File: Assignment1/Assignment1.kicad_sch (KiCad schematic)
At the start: 22 parts, among them J1 Conn_01x02_Pin, J2 Conn_01x02_Pin, U1 TPS51386RJNR, U2 LD39200PU33R

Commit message: Update Assignment 1
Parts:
- removed Cbyp1: 470 nF, Capacitor_SMD:C_0603_1608Metric, symbol Device:C
- removed Cin1, Cout1: 10 uF, Capacitor_SMD:C_0603_1608Metric, symbol Device:C
- removed R_LDO_1: 56k, Resistor_SMD:R_0603_1608Metric, symbol Device:R
- removed R_LDO_2: 10k, Resistor_SMD:R_0603_1608Metric, symbol Device:R
- removed U2: LD39200PU33R, LD39200PU33R:SON95P300X300X100-7N, symbol LD39200PU33R:LD39200PU33R
- added C2, C3, C8: 22pF, Capacitor_SMD:C_1210_3225Metric, symbol Device:C
- added Cbyp2: 47 uF, Capacitor_SMD:C_1206_3216Metric, symbol Device:C
- added Cin2: 1 uF, Capacitor_SMD:C_0603_1608Metric, symbol Device:C
- added U3: ~, Package_TO_SOT_SMD:TO-263-3_TabPin2, symbol ProLib_pcs_2025-01-30:LM39300R-3.3
- C12: footprint Capacitor_SMD:C_0603_1608Metric -> Capacitor_SMD:C_1210_3225Metric
- C4, C5: footprint Capacitor_SMD:C_0603_1608Metric -> Capacitor_SMD:C_1206_3216Metric
- C7: value 100uF -> 22pF; footprint Capacitor_SMD:C_0603_1608Metric -> Capacitor_SMD:C_1210_3225Metric
- J1, J2: footprint Connector_PinSocket_2.54mm:PinSocket_1x02_P2.54mm_Vertical -> 5EHDVC-02P-KiCad:5EHDVC02P
- R4: value 150k -> 110k
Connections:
- net BuckStep_Vout: now also C2.1, C3.1, C8.1, Cin2.1, U3.1 (VIN)
- net Earth: now also C2.2, C3.2, C8.2, Cbyp2.2, Cin2.2, U3.2 (GND), U3.4 (TAB)
- net Vout: now also Cbyp2.1, U3.3 (VOUT)
- no-connect marks 2 -> 1
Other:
- note added: "LDO Module Converts 3.9V to 3.3V at maximum 2A"
- note removed: "LDO Module Converts 5.1V to 3.3V at maximum 2A"

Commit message: fix typo and update pcb
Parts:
- C2, C3, C7, C8: value 22pF -> 22uF
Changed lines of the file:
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@@
 		(on_board yes)
 		(dnp no)
-		(fields_autoplaced yes)
 		(property "Reference" "C8"
-			(at 123.19 90.1699 0)
+			(at 120.904 89.154 0)
 			(effects
 				(font
@@
 			)
 		)
-		(property "Value" "22pF"
-			(at 123.19 92.7099 0)
+		(property "Value" "22uF"
+			(at 120.396 93.726 0)
 			(effects
 				(font
@@
 		(on_board yes)
 		(dnp no)
-		(fields_autoplaced yes)
 		(property "Reference" "C7"
-			(at 116.84 90.1699 0)
+			(at 113.792 89.408 0)
 			(effects
 				(font
@@
 			)
 		)
-		(property "Value" "22pF"
-			(at 116.84 92.7099 0)
+		(property "Value" "22uF"
+			(at 113.538 93.726 0)
 			(effects
 				(font
@@
 		(on_board yes)
 		(dnp no)
-		(fields_autoplaced yes)
 		(property "Reference" "C3"
-			(at 138.43 90.1699 0)
+			(at 136.398 89.154 0)
 			(effects
 				(font
@@
 			)
 		)
-		(property "Value" "22pF"
-			(at 138.43 92.7099 0)
+		(property "Value" "22uF"
+			(at 136.398 93.98 0)
 			(effects
 				(font
@@
 		(on_board yes)
 		(dnp no)
-		(fields_autoplaced yes)
 		(property "Reference" "C2"
-			(at 129.54 90.1699 0)
+			(at 127.254 89.154 0)
 			(effects
 				(font
@@
 			)
 		)
-		(property "Value" "22pF"
-			(at 129.54 92.7099 0)
+		(property "Value" "22uF"
+			(at 126.746 93.726 0)
 			(effects
 				(font

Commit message: reformat
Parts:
- C13, Cin2: value 1 uF -> 1uF
- C4, C5: value 10 uF -> 10uF
- C6: value 0.1 uF -> 0.1uF
- Cbyp2: value 47 uF -> 47uF
- R3: value 100 k -> 100k
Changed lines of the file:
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@@
 		(on_board yes)
 		(dnp no)
-		(fields_autoplaced yes)
 		(property "Reference" "C13"
-			(at 77.47 35.56 90)
+			(at 77.47 36.576 90)
 			(effects
 				(font
@@
 			)
 		)
-		(property "Value" "1 uF"
-			(at 77.47 38.1 90)
+		(property "Value" "1uF"
+			(at 77.47 39.116 90)
 			(effects
 				(font
@@
 		(on_board yes)
 		(dnp no)
-		(fields_autoplaced yes)
 		(property "Reference" "R5"
-			(at 91.44 93.98 90)
+			(at 91.44 95.758 90)
 			(effects
 				(font
@@
 		)
 		(property "Value" "0"
-			(at 91.44 96.52 90)
+			(at 91.44 98.298 90)
 			(effects
 				(font
@@
 		(on_board yes)
 		(dnp no)
-		(fields_autoplaced yes)
 		(property "Reference" "C5"
-			(at 91.44 27.94 0)
+			(at 90.424 27.432 0)
 			(effects
 				(font
@@
 			)
 		)
-		(property "Value" "10 uF"
-			(at 91.44 30.48 0)
+		(property "Value" "10uF"
+			(at 90.424 30.48 0)
 			(effects
 				(font
@@
 		(on_board yes)
 		(dnp no)
-		(fields_autoplaced yes)
 		(property "Reference" "C12"
-			(at 101.6 92.71 90)
+			(at 101.6 94.234 90)
 			(effects
 				(font
@@
 		)
 		(property "Value" "22pF"
-			(at 101.6 95.25 90)
+			(at 101.6 96.774 90)
 			(effects
 				(font
@@
 		(on_board yes)
 		(dnp no)
-		(fields_autoplaced yes)
 		(property "Reference" "R4"
-			(at 96.52 85.09 90)
+			(at 96.52 86.36 90)
 			(effects
 				(font
@@
 		)
 		(property "Value" "110k"
-			(at 96.52 87.63 90)
+			(at 96.52 88.9 90)
 			(effects
 				(font
@@
 		(fields_autoplaced yes)
 		(property "Reference" "C6"
-			(at 101.6 27.94 0)
+			(at 101.6 27.9399 0)
 			(effects
 				(font
@@
 			)
 		)
-		(property "Value" "0.1 uF"
-			(at 101.6 30.48 0)
+		(property "Value" "0.1uF"
+			(at 101.6 30.4799 0)
 			(effects
 				(font
@@
 		(fields_autoplaced yes)
 		(property "Reference" "C4"
-			(at 80.01 27.94 0)
+			(at 80.01 27.9399 0)
 			(effects
 				(font
@@
 			)
 		)
-		(property "Value" "10 uF"
-			(at 80.01 30.48 0)
+		(property "Value" "10uF"
+			(at 80.01 30.4799 0)
 			(effects
 				(font
@@
 		(fields_autoplaced yes)
 		(property "Reference" "Cbyp2"
-			(at 220.98 57.15 0)
+			(at 220.98 57.1499 0)
 			(effects
 				(font
@@
 			)
 		)
-		(property "Value" "47 uF"
-			(at 220.98 59.69 0)
+		(property "Value" "47uF"
+			(at 220.98 59.6899 0)
 			(effects
 				(font
@@
 		(fields_autoplaced yes)
 		(property "Reference" "Cin2"
-			(at 199.39 48.26 0)
+			(at 199.39 48.2599 0)
 			(effects
 				(font
@@
 			)
 		)
-		(property "Value" "1 uF"
-			(at 199.39 50.8 0)
+		(property "Value" "1uF"
+			(at 199.39 50.7999 0)
 			(effects
 				(font
@@
 			)
 		)
-		(property "Value" "100 k"
+		(property "Value" "100k"
 			(at 77.47 49.53 90)
 			(effects

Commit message: update C 22pf package size to 0603
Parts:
- C12: footprint Capacitor_SMD:C_1210_3225Metric -> Capacitor_SMD:C_0603_1608Metric
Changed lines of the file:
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@@
 			)
 		)
-		(property "Footprint" "Capacitor_SMD:C_1210_3225Metric"
+		(property "Footprint" "Capacitor_SMD:C_0603_1608Metric"
 			(at 105.41 99.3648 0)
 			(effects

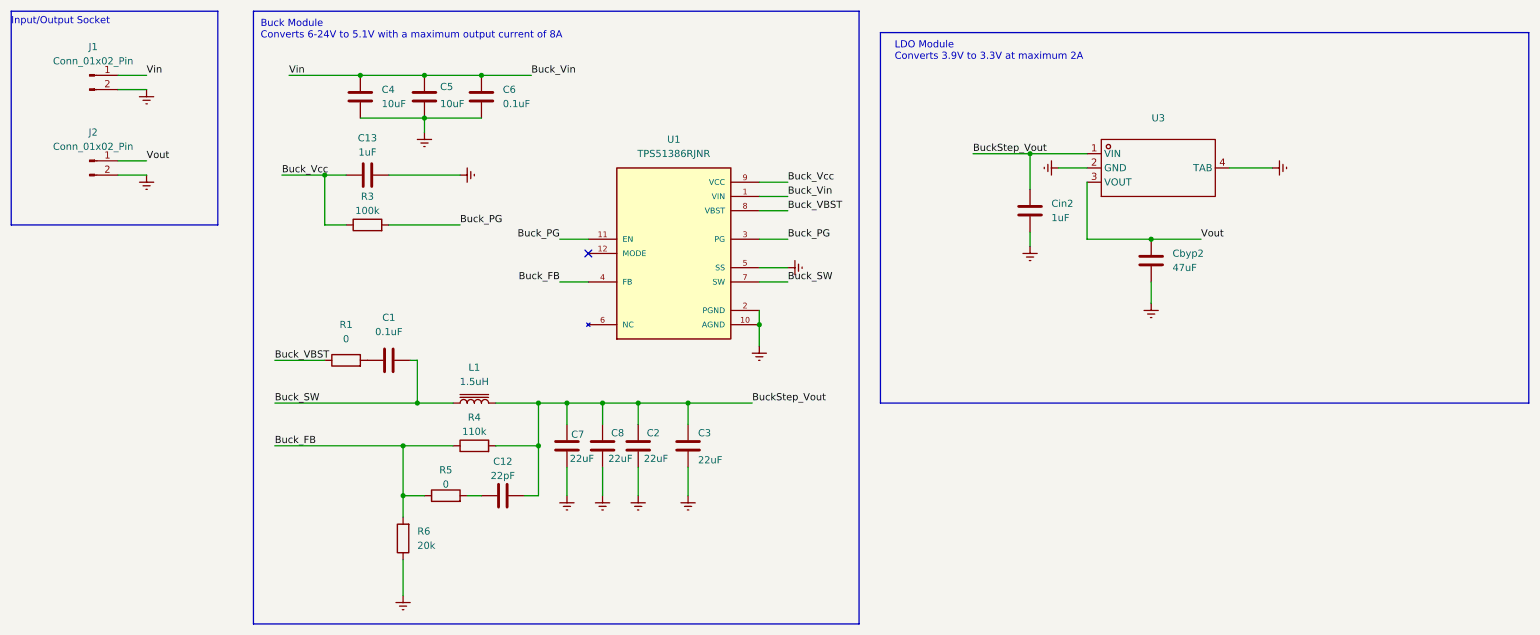
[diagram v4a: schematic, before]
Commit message: assignment1, schematic: update label
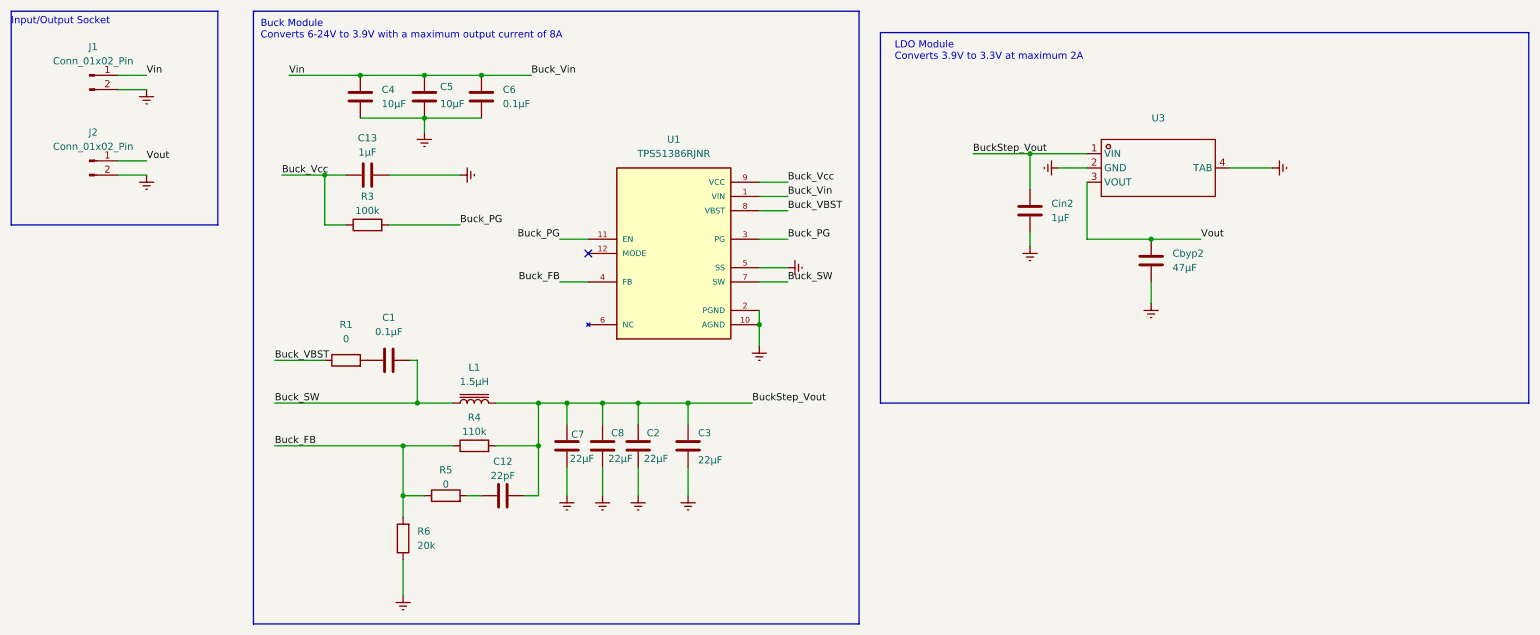
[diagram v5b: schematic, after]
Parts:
- C1, C6: value 0.1uF -> 0.1μF
- C13, Cin2: value 1uF -> 1μF
- C2, C3, C7, C8: value 22uF -> 22μF
- C4, C5: value 10uF -> 10μF
- Cbyp2: value 47uF -> 47μF
- L1: value 1.5uH -> 1.5μH
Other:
- note added: "Buck Module Converts 6-24V to 3.9V with a maximum output current of 8A"
- note removed: "Buck Module Converts 6-24V to 5.1V with a maximum output current of 8A"
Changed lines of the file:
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@@
 		)
 	)
-	(text "Buck Module\nConverts 6-24V to 5.1V with a maximum output current of 8A"
+	(text "Buck Module\nConverts 6-24V to 3.9V with a maximum output current of 8A"
 		(exclude_from_sim no)
 		(at 58.42 19.05 0)
@@
 			)
 		)
-		(property "Value" "1uF"
+		(property "Value" "1μF"
 			(at 77.47 39.116 90)
 			(effects
@@
 			)
 		)
-		(property "Value" "10uF"
+		(property "Value" "10μF"
 			(at 90.424 30.48 0)
 			(effects
@@
 			)
 		)
-		(property "Value" "22uF"
+		(property "Value" "22μF"
 			(at 120.396 93.726 0)
 			(effects
@@
 			)
 		)
-		(property "Value" "0.1uF"
+		(property "Value" "0.1μF"
 			(at 101.6 30.4799 0)
 			(effects
@@
 			)
 		)
-		(property "Value" "10uF"
+		(property "Value" "10μF"
 			(at 80.01 30.4799 0)
 			(effects
@@
 			)
 		)
-		(property "Value" "1.5uH"
+		(property "Value" "1.5μH"
 			(at 96.52 80.01 90)
 			(effects
@@
 			)
 		)
-		(property "Value" "22uF"
+		(property "Value" "22μF"
 			(at 113.538 93.726 0)
 			(effects
@@
 			)
 		)
-		(property "Value" "22uF"
+		(property "Value" "22μF"
 			(at 136.398 93.98 0)
 			(effects
@@
 			)
 		)
-		(property "Value" "22uF"
+		(property "Value" "22μF"
 			(at 126.746 93.726 0)
 			(effects
@@
 			)
 		)
-		(property "Value" "0.1uF"
+		(property "Value" "0.1μF"
 			(at 81.28 71.12 90)
 			(effects
@@
 			)
 		)
-		(property "Value" "47uF"
+		(property "Value" "47μF"
 			(at 220.98 59.6899 0)
 			(effects
@@
 			)
 		)
-		(property "Value" "1uF"
+		(property "Value" "1μF"
 			(at 199.39 50.7999 0)
 			(effects
